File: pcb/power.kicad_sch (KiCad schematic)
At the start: 18 parts, among them J1 UJ20-C-H-G-SMT-P16-TR, Q1 STL11N3LLH6, U2 ECMF02-2AMX6, U4 TCPP01_M12, U6 ST732M33R

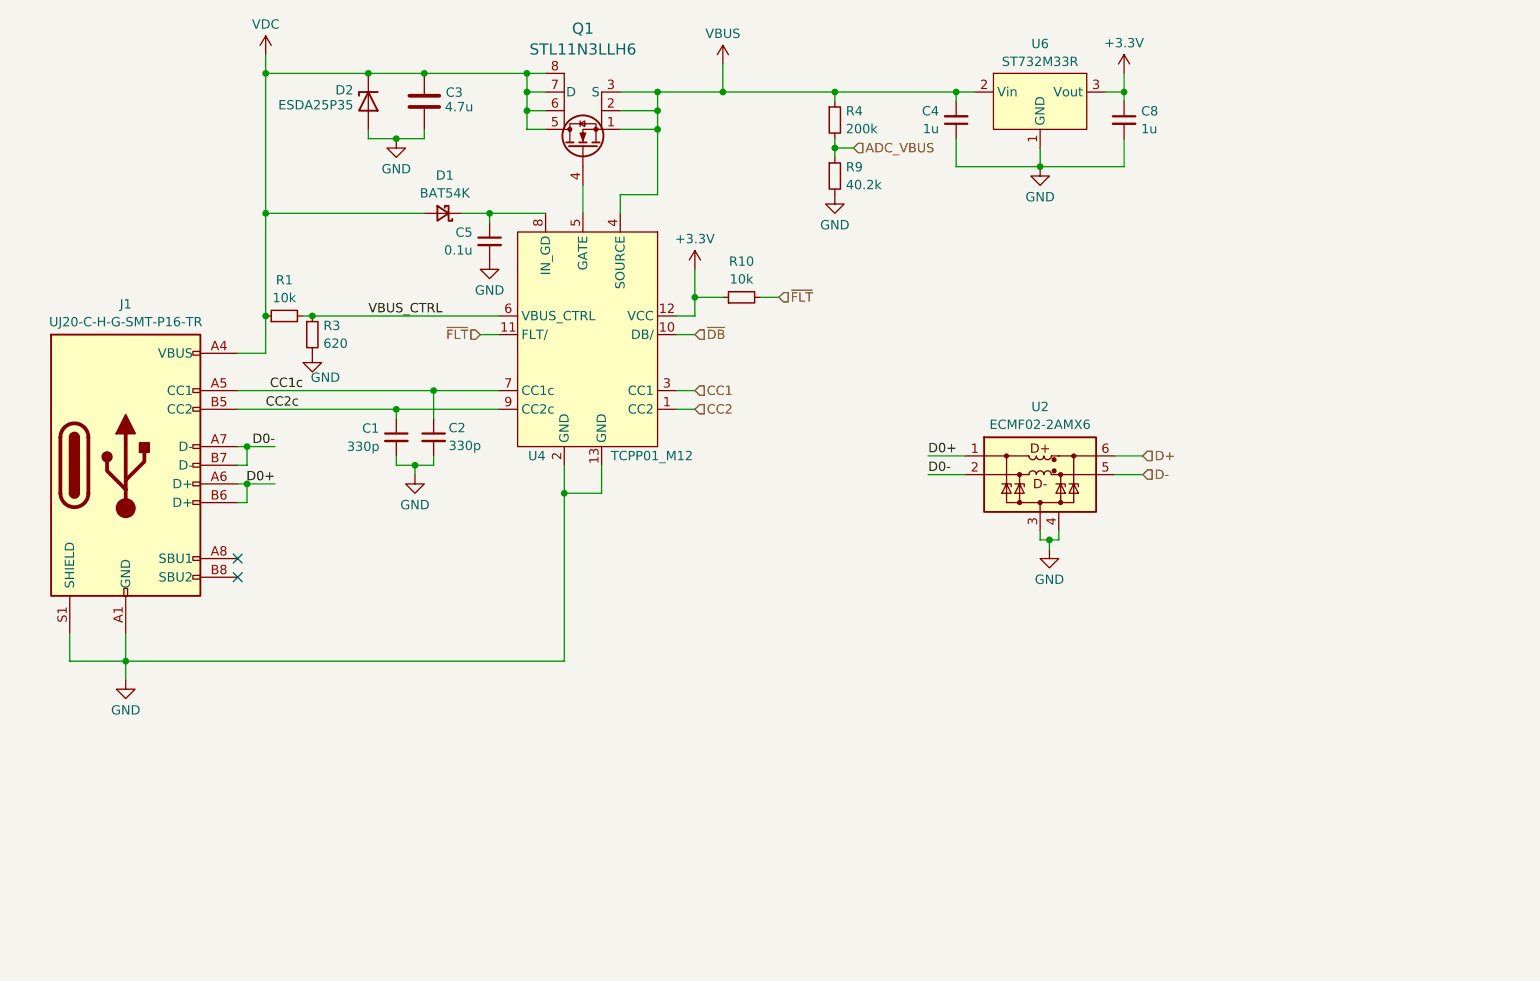
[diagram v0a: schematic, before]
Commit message: finalized schematic v2, add GS cap for inrush current
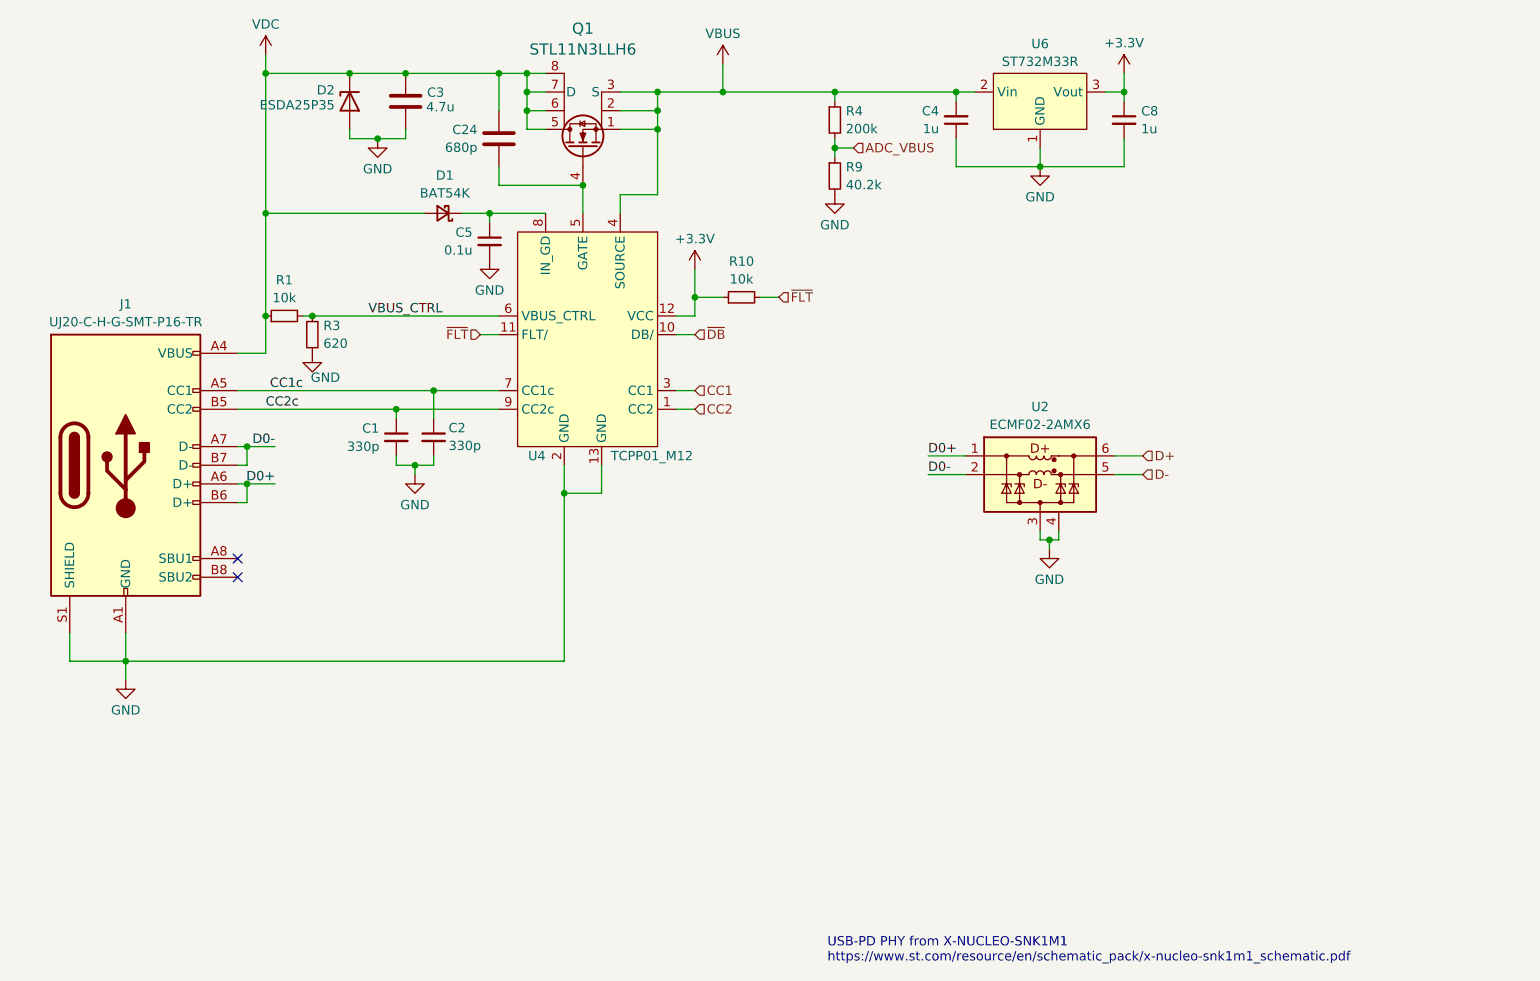
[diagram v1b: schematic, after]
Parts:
- added C24: 680p, Capacitor_SMD:C_0603_1608Metric, symbol Device:C
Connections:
- net VDC: now also C24.1
- net at Q1.4, U4.5 (GATE): now also C24.2
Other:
- note added: "USB-PD PHY from X-NUCLEO-SNK1M1 https://www.st.com/resource/en/schematic_pack/x-nucleo-snk1m1_schematic.pdf"
- moved on the sheet: C3, D2
